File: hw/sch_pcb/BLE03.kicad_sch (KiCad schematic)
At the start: 28 parts, among them J1 HEADER_1x02, J4 Conn_Coaxial, M1 HOLE, M2 HOLE, M3 HOLE, M4 HOLE, U1 CC3301, Y1 TZ3877AAA044, Y2 LFSPXO009682

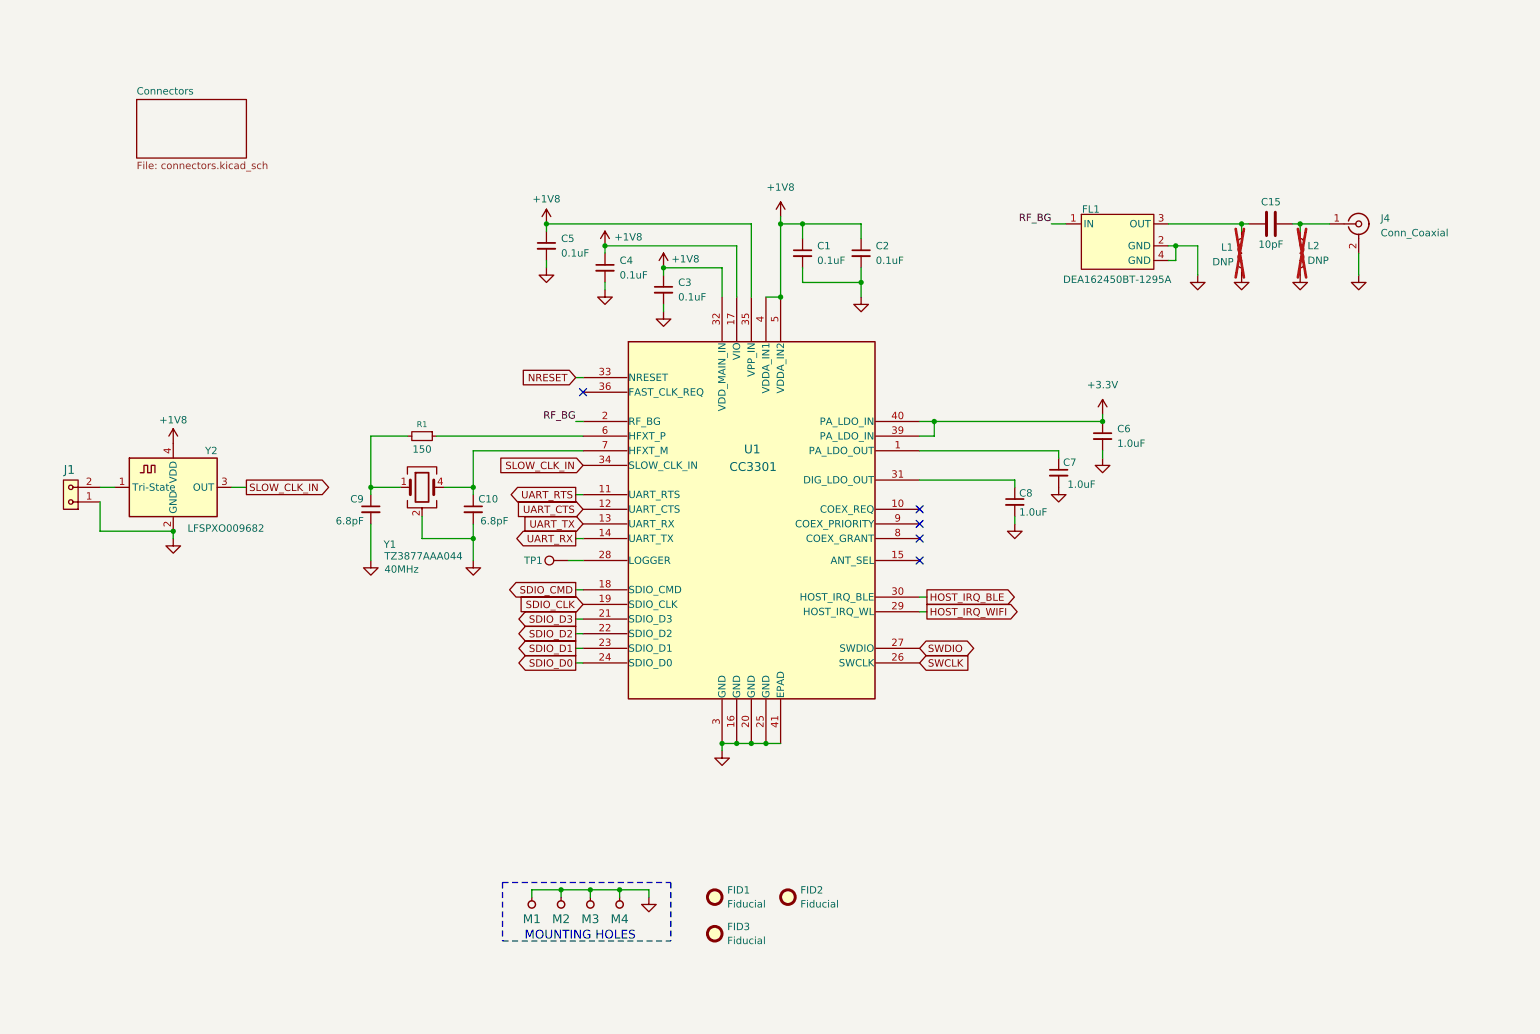
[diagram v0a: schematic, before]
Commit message: Change SAW filter to more available component type.
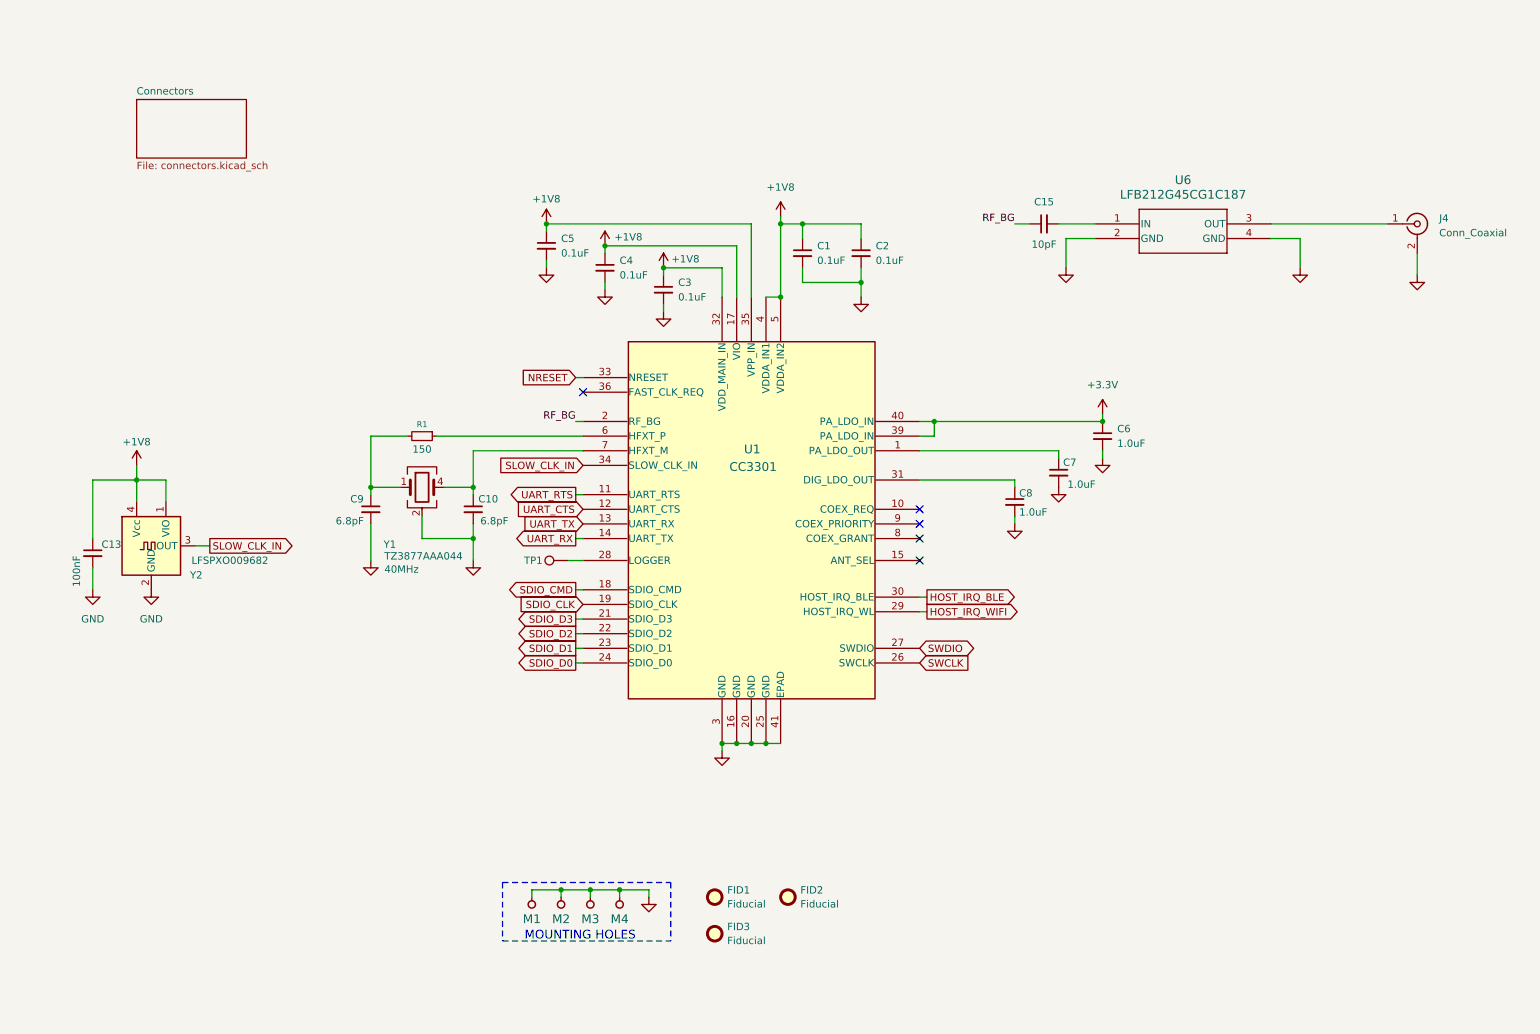
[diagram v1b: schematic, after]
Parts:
- removed FL1: DEA162450BT-1295A, symbol BLE03_lib:DEA162450BT-1295A1
- removed J1: HEADER_1x02, Mlab_Pin_Headers:Straight_1x02, symbol MLAB_HEADER:HEADER_1x02
- removed L1, L2: DNP, Inductor_SMD:L_0603_1608Metric, symbol Device:L
- removed Y2: LFSPXO009682, Oscillator:Oscillator_SMD_Abracon_ASCO-4Pin_1.6x1.2mm, symbol Oscillator:ASCO
- added C13: 100nF, Capacitor_SMD:C_0603_1608Metric, symbol Device:C_Small
- added U6: LFB212G45CG1C187, MLAB_SAW:Murata_C187, symbol MLAB_Lib:LFB212G45CG1C187
- added Y2: LFSPXO009682, Oscillator:Oscillator_SMD_SeikoEpson_SG210-4Pin_2.5x2.0mm, symbol Oscillator:SG-3030CM
- C15: symbol Device:C -> Device:C_Small
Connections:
- net +1V8: now also C13.1, Y2.1 (VIO), Y2.4 (Vcc)
- net GND: now also C13.2, U6.2 (GND), U6.4 (GND), Y2.2 (GND)
- net RF_BG: now also C15.1
- net SLOW_CLK_IN: now also Y2.3 (OUT)
- net at J4.1 (In): now also U6.3 (OUT); no longer C15.2
- new net: C15.2, U6.1 (IN)
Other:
- moved on the sheet: C15, J4

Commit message: Documentation cleanup.
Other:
- note added: "Tady možná bude potřeba nějaký RC člen kvůli spoždění resetu po zapnutí napájení."
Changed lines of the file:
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@@
 		(company "MLAB")
+	)
+	(text "Tady možná bude potřeba nějaký RC člen kvůli spoždění resetu po zapnutí napájení."
+		(exclude_from_sim no)
+		(at 64.77 74.93 0)
+		(effects
+			(font
+				(size 1.27 1.27)
+			)
+		)
 	)
 	(text "MOUNTING HOLES"

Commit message: Adding connectors and other components
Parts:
- removed C13: 100nF, Capacitor_SMD:C_0603_1608Metric, symbol Device:C_Small
- removed R1: 150, Resistor_SMD:R_0603_1608Metric, symbol Device:R_Small
- removed U6: LFB212G45CG1C187, MLAB_SAW:Murata_C187, symbol MLAB_Lib:LFB212G45CG1C187
- removed Y1: TZ3877AAA044, symbol Device:Crystal_GND23
- removed Y2: LFSPXO009682, Oscillator:Oscillator_SMD_SeikoEpson_SG210-4Pin_2.5x2.0mm, symbol Oscillator:SG-3030CM
- added C1: 10uF, Capacitor_SMD:C_0603_1608Metric, symbol Device:C
- added C2: 100nF, Capacitor_SMD:C_0603_1608Metric, symbol Device:C
- added C3: 1uF, Mlab_R:SMD-0603, symbol Device:C
- added D1: BZX585-B5V6.115, Diode_SMD:D_SOD-523, symbol MLAB_D:D_ZENER
- added D2: LED, LED_SMD:LED_0805_2012Metric, symbol Device:LED
- added FL1: DEA162450BT-1295A, Filter_custom:RF_1260B3_TDK, symbol BLE03_lib:DEA162450BT-1295A1
- added J1: 3V3, Mlab_Pin_Headers:Straight_2x03, symbol MLAB_HEADER:HEADER_2x03_PARALLEL
- added L1, L2: DNP, Inductor_SMD:L_0603_1608Metric, symbol Device:L
- added R1: 2k2, Resistor_SMD:R_0603_1608Metric, symbol cc2564-board-rescue:R-Device
- added U1: MIC5504-1.8YM5, Package_TO_SOT_SMD:SOT-23-5, symbol Regulator_Linear:MIC5504-1.8YM5
- added Y1: ABM8AIG-40.000MHZ-12-2Z-T3, Crystal:Crystal_SMD_Abracon_ABM8AIG-4Pin_3.2x2.5mm, symbol Device:Crystal_GND24
- added Y2: LFSPXO009682, Oscillator:Oscillator_SMD_Abracon_ASCO-4Pin_1.6x1.2mm, symbol Oscillator:ASCO
- C13: renamed from C9; value 6.8pF -> 4pF
- C14: renamed from C10; value 6.8pF -> 4pF
- C9: renamed from C15; symbol Device:C_Small -> Device:C
- TP1: footprint TestPoint:TestPoint_Pad_D1.0mm -> TestPoint:TestPoint_Pad_D1.5mm
- renumbered C6 to C10, C7 to C11, C8 to C12, C5 to C4, C1 to C5, C2 to C6, C4 to C7, C3 to C8, J4 to J2, U1 to U2
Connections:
- net +1V8: now also C3.1, U1.5 (VOUT), Y2.4 (VDD)
- net GND: now also C1.2, C2.2, C3.2, D1.2 (A), D2.1 (K), FL1.2 (GND), FL1.4 (GND), J1.1, J1.2, J1.5, J1.6, L1.1, L2.2, U1.2 (GND), Y1.2 (G), Y1.4 (G), Y2.2 (GND)
- net RF_BG: now also FL1.1 (IN); no longer C9.1
- net SLOW_CLK_IN: now also Y2.3 (OUT)
- net at J2.1 (In): now also C9.2, L2.1
- net at U2.6 (HFXT_P): now also C13.1, Y1.1
- net at C14.1, U2.7 (HFXT_M): now also Y1.3
- new net: C9.1, FL1.3 (OUT), L1.2
- new net: D2.2 (A), R1.2
- new net +3V3: C1.1, C2.1, D1.1 (K), J1.3, J1.4, R1.1, U1.1 (VIN), U1.3 (EN)
- no-connect marks 5 -> 6
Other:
- note added: "POWER"
- note removed: "Tady možná bude potřeba nějaký RC člen kvůli spoždění resetu po zapnutí napájení."
- moved on the sheet: C10, C11, C12, C13, C14, C4, C5, C6, C7, C8, C9, FID1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

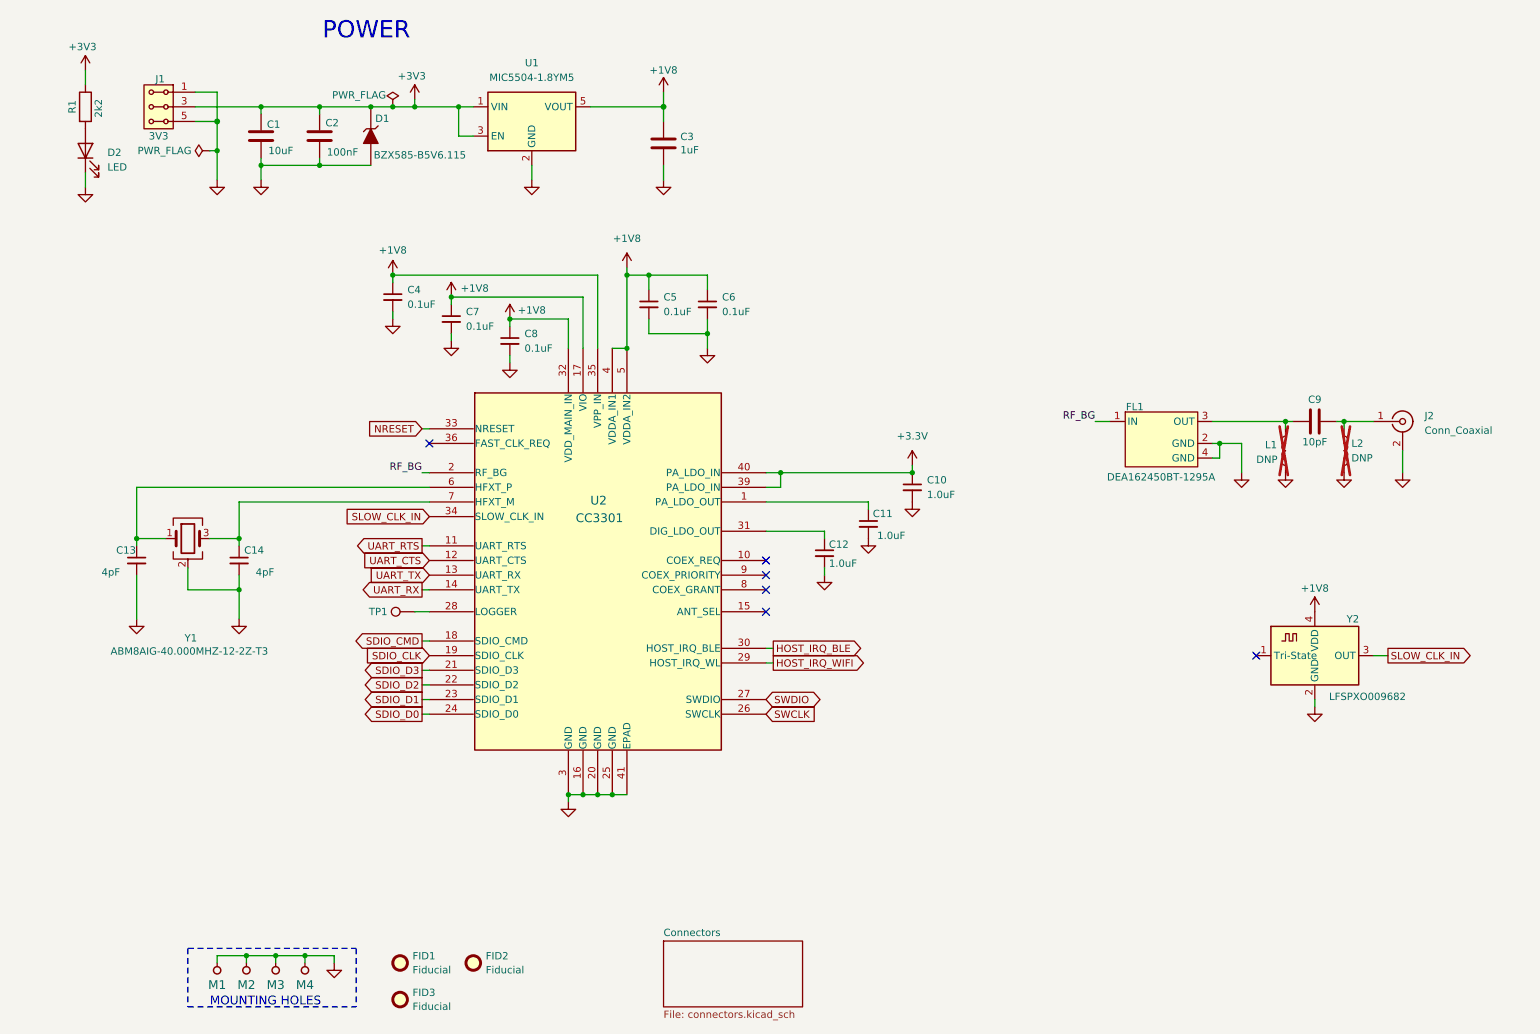
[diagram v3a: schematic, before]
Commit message: Improving sch and adding RC filter for reset line
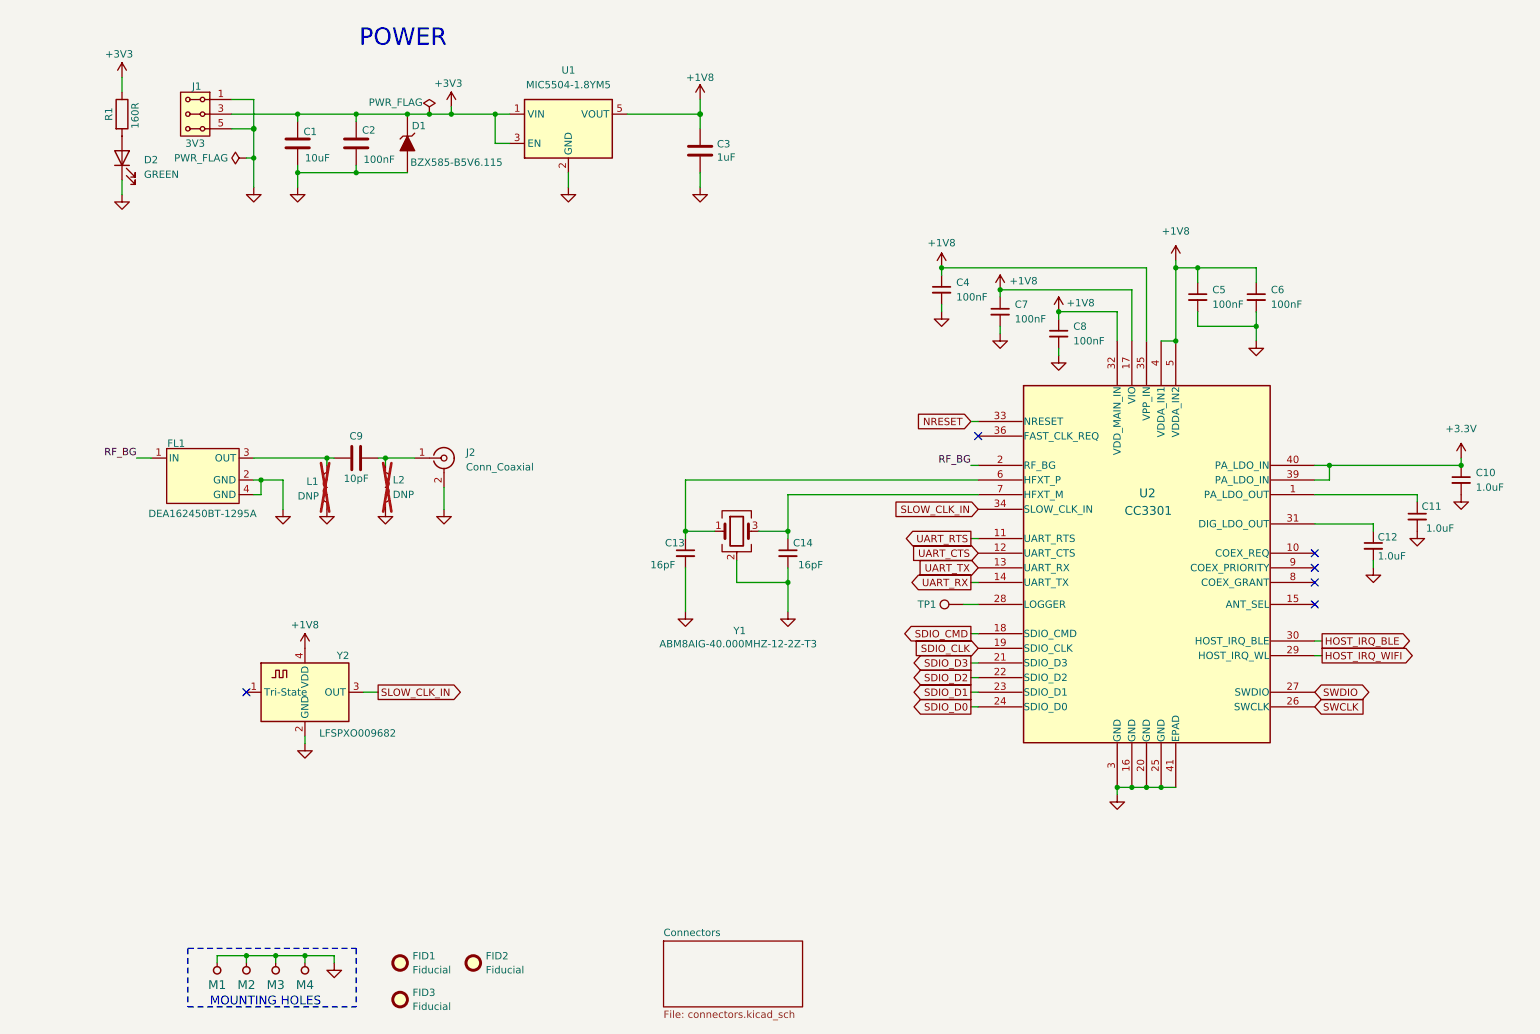
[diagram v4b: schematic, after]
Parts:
- C13, C14: value 4pF -> 16pF
- C4, C5, C6, C7, C8: value 0.1uF -> 100nF
- D2: value LED -> GREEN
- R1: value 2k2 -> 160R
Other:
- moved on the sheet: C1, C10, C11, C12, C13, C14, C2, C3, C4, C5, C6, C7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
